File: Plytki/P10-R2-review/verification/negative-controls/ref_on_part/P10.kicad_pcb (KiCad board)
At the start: 2 copper layers, 53 x 100 mm, 24 parts, among them J1 J_BP, J2 SERWIS, J3 OBD, U1 TCAN1051V, U2 74LVC125AD

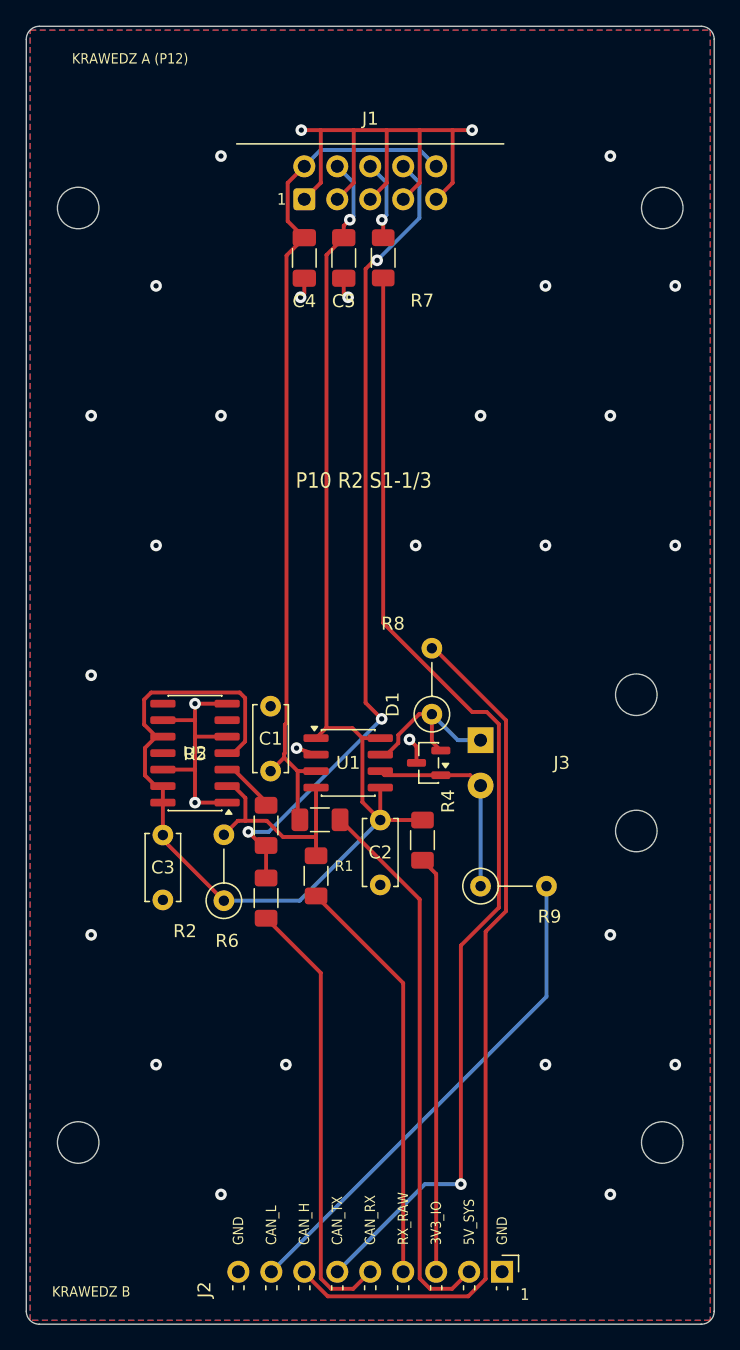
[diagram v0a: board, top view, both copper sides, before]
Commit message: P10 R2 PCB: poprawki po recenzji (CAN przez D1, pierścień wokół J3, nadruk, kontrole)
- CAN_H / CAN_L zablokowane z J3 przez pola D1 do U1 (było: CAN_H do D1
  odgałęzieniem 3 mm); obejście D1 1,4 mm zostawia miejsce na przelotkę
  GND D1.3; korytarz linii wolny przy rozmieszczaniu
- pierścień 1 mm bez innej miedzi wokół lutowanych pól J3 (F.Cu z kanałem
  dla linii do D1, B.Cu pełny); było SRV_CAN_TX 0,26 mm od pól
- nadruk: oznaczenie zawsze bliżej swojej części, tytuł ze slotem
  (S1 §9), „H”/„L” przy polach J3; ukryte oznaczenia na rysunku z F.Fab
- kontrole: przez D1, odstęp od pól J3, pas A (S1 §5), najbliższy obrys,
  znaczniki, etykiety z tabeli LABEL; próby ujemne 24/24 (+6)
- PDF: podpis renderu bez modeli 3D, liczebniki, stopka; teksty ZAKUPY,
  QA, README, WIAZKI (punkt widzenia „po prawej”)
- DRC 0/0/0, kontrole PCB 24/24

Co-Authored-By: Claude Opus 5.5 <noreply@anthropic.com>
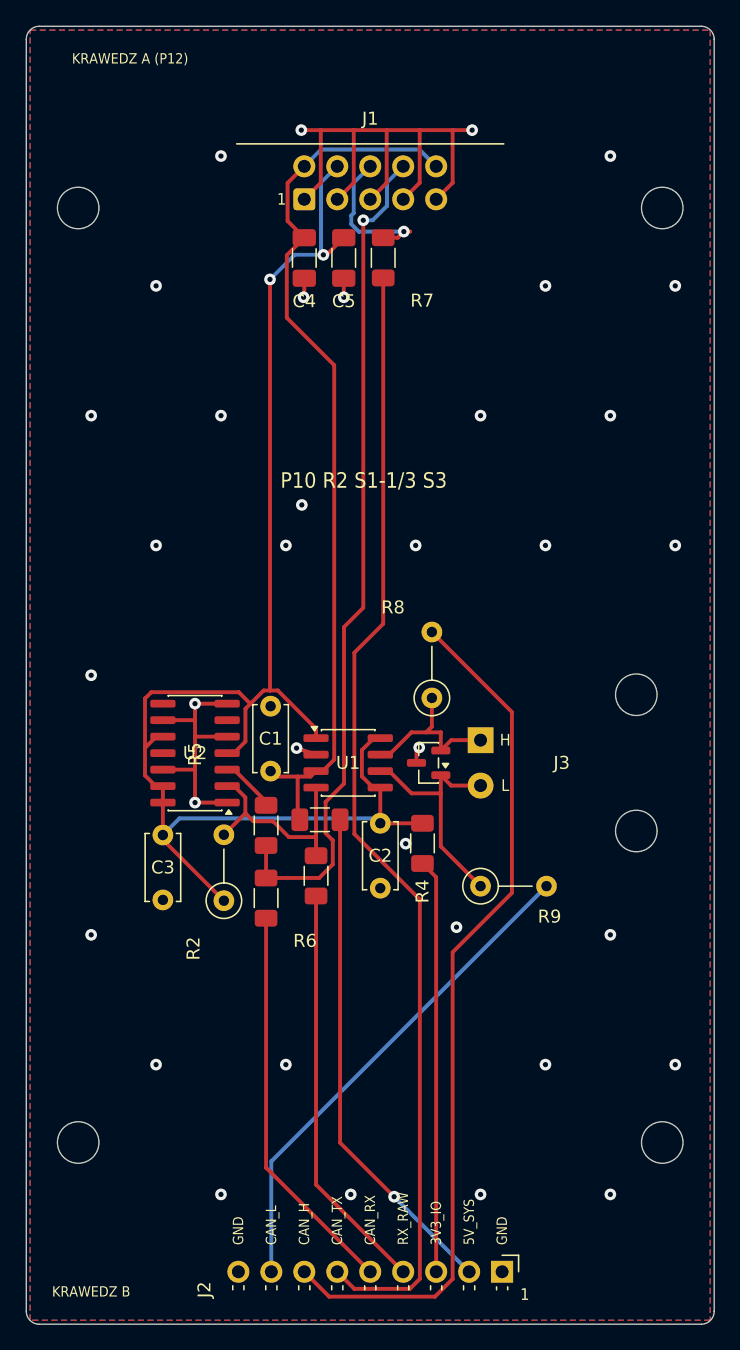
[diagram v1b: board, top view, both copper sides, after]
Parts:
- moved R8 1.25 mm to (31.2, 51.8)
- moved C2 0.25 mm to (27.3, 61.4)
- moved R4 0.25 mm to (30.5, 63.0)
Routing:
- net 3V3_IO: track 110.4 -> 116.3 mm, vias 1 -> 2
- net /CORE/CAN_TX: track 6.21 -> 11.6 mm
- net /CORE/SRV_CAN_RX: track 34.2 -> 30.6 mm
- net /CORE/SRV_5V_SYS: track 42.6 -> 38.9 mm, vias 0 -> 1
- net CAN_L: track 15.9 -> 18.6 mm
- net 5V_SYS: track 66.6 -> 69.1 mm
- net /CORE/CAN_RX: track 63.9 -> 65.0 mm, vias 3 -> 1
- net GND: track 69.2 -> 68.2 mm, vias 30 -> 36
- net /CORE/SRV_CAN_TX: track 87.7 -> 87.4 mm, vias 1 -> 0
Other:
- board text added: "H"
- board text added: "L"
- board text added: "P10 R2 S1-1/3 S3"
- board text removed: "P10 R2 S1-1/3"
